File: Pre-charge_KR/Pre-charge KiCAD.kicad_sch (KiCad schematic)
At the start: 56 parts, among them IC1 AL5890-10D-13, IC2 TLV1701AIDBVT, J1 Conn_01x02, J113 Conn_01x06, J3 Conn_01x02, J4 Conn_01x02, K2 G5Q-1A4-DC12, K3 67-1-A-12/2D, Q1 2N7000, Q2 2N7000, Q4 2N7000, U1 HCPL-817-000E, U10 LM7805MPX/NOPB, U13 HCPL-817-000E, U2 LM339N/NOPB, U3 SN74AHCT1G08DBVR, U7 LM741CN/NOPB, U8 SN74AHC1G04DBVRE4

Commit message: breakout updated and ENNOID BMS added
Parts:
- removed Q1: 2N7000, Package_TO_SOT_THT:TO-92_Inline, symbol Transistor_FET:2N7000
- removed R11: 10k, Resistor_THT:R_Axial_DIN0207_L6.3mm_D2.5mm_P10.16mm_Horizontal, symbol Device:R_Small
- removed R9: 100, Resistor_THT:R_Axial_DIN0207_L6.3mm_D2.5mm_P10.16mm_Horizontal, symbol Device:R_Small
- renumbered J113 to J2
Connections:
- net Precharge_done/Close_AIR1: now also R8.1, U2.13
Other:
- note added: "AIR close should be shutdown ok and RTD OK and Precharge done"
- note added: "I have a feeling this relay resistor order is incorrect"
- note added: "Is this necessary or just good to have? theres no teensy monitoring pins setup right now for this"
- note added: "Precharge enable should be SDWN_PC and RTD and PC not done"
- note added: "Think this is a debug pin, but its the wrong voltage"
- note added: "This comes from Teensy"
- note added: "This goes to the AIR"
- note added: "This goes to the TSAL"
- note added: "This is end of shutdown circuit daisy chain"
- note added: "This should be 3.3V to not blow the Teensy"
- moved on the sheet: C10, C11, C2, C7, J2, J3, R24, U10, U8

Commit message: precharge complete
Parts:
- removed C1, C11: 0.1uF, FA14_Capacitor:FA18X7R1H104KNU00, symbol Device:C
- removed C2: 10uF, Capacitor_THT:CP_Radial_D5.0mm_P2.50mm, symbol Device:C_Polarized
- removed C4: 0.1uF, FA14_Capacitor:FA18X7R1H104KNU00, symbol Device:C_Small
- removed C7: 0.22uF, FA14_Capacitor:FA14X7R1H224KNU00, symbol Device:C
- removed D1: TZX3V9C-TAP, Diode_THT:D_DO-35_SOD27_P7.62mm_Horizontal, symbol Diode:BZX384-xxx
- removed D3: TZX3V0B-TR, Diode_THT:D_DO-35_SOD27_P7.62mm_Horizontal, symbol Diode:BZX384-xxx
- removed IC1: AL5890-10D-13, AL589010D13:AL589010D13, symbol AL5890-10D-13:AL5890-10D-13
- removed LED1: LTL-1CHG, LTL1CHG:LTL1CHG, symbol LTL-1CHG:LTL-1CHG
- removed R12: 20k, Resistor_THT:R_Axial_DIN0207_L6.3mm_D2.5mm_P10.16mm_Horizontal, symbol Device:R_Small
- removed R24: 1M, Resistor_THT:R_Axial_DIN0207_L6.3mm_D2.5mm_P10.16mm_Horizontal, symbol Device:R_Small
- removed R36: 6.8k, Resistor_THT:R_Axial_DIN0207_L6.3mm_D2.5mm_P10.16mm_Horizontal, symbol Device:R_Small
- removed R37: 4.7k, Resistor_THT:R_Axial_DIN0207_L6.3mm_D2.5mm_P10.16mm_Horizontal, symbol Device:R_Small
- removed U10: LM7805MPX/NOPB, Package_TO_SOT_SMD:SOT-223-3_TabPin2, symbol Regulator_Linear:LM7805_TO220
- removed U2: LM339N/NOPB, LM339N:DIP794W53P254L1930H508Q14N, symbol Comparator:LM339
- removed U3: SN74AHCT1G08DBVR, Package_TO_SOT_SMD:SOT-23-5, symbol 74xGxx:74AHC1G08
- removed U7: LM741CN/NOPB, Package_DIP:DIP-8_W7.62mm, symbol Amplifier_Operational:LM741
- added C1, C4: 1uF, FA14_Capacitor:FA18X7R1H104KNU00, symbol tsal-rescue:C_Small-Device
- added C2: 0.1uF, FA14_Capacitor:FA18X7R1H104KNU00, symbol Device:C
- added C5: 2.2uF, FA14_Capacitor:FA14X7R1H224KNU00, symbol Device:C_Small
- added D1: 1N4001, Diode_THT:D_DO-41_SOD81_P10.16mm_Horizontal, symbol Device:D
- added D2, D3: 1N4148, Diode_THT:D_DO-35_SOD27_P7.62mm_Horizontal, symbol Diode:1N4148
- added IC3: SN74LVC1G11DCKRE4, SOT65:SOT65P210X110-6N, symbol SN74LVC1G11DCKRE4:SN74LVC1G11DCKRE4
- added IC4: SN74LVC1G08IDCKRQ1, AND:SOT65P210X110-5N, symbol SN74LVC1G08IDCKRQ1:SN74LVC1G08IDCKRQ1
- added R10, R9: 56k, Resistor_THT:R_Axial_DIN0411_L9.9mm_D3.6mm_P12.70mm_Horizontal, symbol Device:R_Small
- added R11: 330, Resistor_THT:R_Axial_DIN0207_L6.3mm_D2.5mm_P10.16mm_Horizontal, symbol Device:R_Small
- added R3, R6: 100k, Resistor_THT:R_Axial_DIN0207_L6.3mm_D2.5mm_P10.16mm_Horizontal, symbol Device:R_Small
- added U2: MCP1703AT-3302E/MBVAO, Package_TO_SOT_SMD:SOT-89-3, symbol Regulator_Linear:MCP1703Ax-300xxMB
- J3: footprint Phoenix 1x2 Connector:Phoenix_1x2_1729128 -> Connector_JST:JST_XH_B2B-XH-A_1x02_P2.50mm_Vertical; Part Number 1729128 -> B6B-XH-A
- R1: value 1.5k -> 100k; Part Number MCF 0.25W 1K5 -> MCF 0.25W 100K
- R2: value 1.5k -> 1M; Part Number MCF 0.25W 1K5 -> MCF 0.25W 1M
- R32, R33, R7: value 10k -> 100k; Part Number MCF 0.25W 10K -> MCF 0.25W 100K
- R34: value 180k -> 1.8M; Part Number MCF 0.25W 180K -> MCF 0.25W 1.8M
- R35: value 1k -> 2.2k; Part Number MCF 0.25W 1K -> MCF 0.25W 2.2k
- R4: value 6.8k -> 10k; Part Number MCF 0.25W 6K8 -> MCF 0.25W 10k
- R5: value 4.7k -> 27k; Part Number MCF 0.25W 4K7 -> MCF 0.25W 27K
- R8: value 10k -> 56k; footprint Resistor_THT:R_Axial_DIN0207_L6.3mm_D2.5mm_P10.16mm_Horizontal -> Resistor_THT:R_Axial_DIN0411_L9.9mm_D3.6mm_P12.70mm_Horizontal; Part Number MCF 0.25W 10K -> MCF 0.5W 56K
- U8: value SN74AHC1G04DBVRE4 -> SN74LVC1G04QDBVRQ1; Part Number SN74AHC1G04DBVRE4 -> SN74LVC1G04QDBVRQ1
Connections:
- net 3Vref is gone; now on an unnamed net: R2.2
- net 12V_HV: now also R4.2
- net GLV+: now also C4.1, U2.2 (VI); no longer R1.1, R2.1, U1.4, U13.4
- net GND: now also J2.3 (Pin_3), R1.1, R7.1, C1.2, C2.2, C4.2, C5.1, IC3.2 (GND), IC4.3 (GND), R3.1, U2.1 (GND); no longer J2.6 (Pin_6), R5.2
- net PRE_RESIST+: now also R8.1
- net Precharge NOT done: now also U8.4, IC4.2 (B); no longer Q4.2 (G)
- net Precharge_ON: now also J2.6 (Pin_6), U1.3, R3.2; no longer J2.1 (Pin_1), R7.1
- net SDWN_PC: now also R5.2, D1.1 (K)
- net Shutdown_AIR1+: now also J2.1 (Pin_1); no longer J2.3 (Pin_3)
- net TS-: now also U1.2, D3.2 (A); no longer U13.2
- net Precharge_done: now reaches U13.3
- net Precharge_done: now also J2.4 (Pin_4), R1.2, U8.2, IC3.1 (A)
- net at R35.1, U13.1: no longer IC2.4 (OUT)
- net at R30.2, R31.1: now also IC2.3 (IN-); no longer IC2.1 (IN+)
- net at R32.1: now also R28.2, R29.1
- net at R32.2, R33.1: now also IC2.1 (IN+), R2.1; no longer IC2.3 (IN-)
- net at R13.2: now also R5.1, IC3.3 (B)
- net at R23.1: now also IC3.4 (Y)
- net at K3.3, Q4.3 (D): now also D1.2 (A)
- net at U1.1: now also D3.1 (K), R11.1
- net at R4.1: now also IC2.4 (OUT), U13.2; no longer U1.3
- removed net 3V9: R1.2, R7.2, R8.2
- net 5V renamed 3.3V
- net 3.3V: now also U1.4, U13.4, C1.1, C2.1, IC3.5 (VCC), IC4.5 (VCC), U2.3 (VO)
- removed net Precharge_done/Close_AIR1: J2.4 (Pin_4), R8.1, U8.2
- net TS_activate renamed Precharge_EN
- net Precharge_EN: now also IC3.6 (C), IC4.1 (A)
- new net: C5.2, D2.1 (K), Q4.2 (G), R6.1, R7.2
- new net: R8.2, R9.1
- new net: R10.1, R9.2
- new net: R10.2, R11.2
- new net: D2.2 (A), IC4.4 (Y), R6.2
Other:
- note added: "AIR_CLOSE_EN = SDC_OK AND RTD_OK AND PC_DONE"
- note added: "Isolated DCDC converter"
- note added: "PC_RELAY_EN = SDC_OK AND RTD_OK AND NOT PC_DONE"
- note added: "Preresist- is the node between resistor and motor inverter capacitor"
- note added: "This delay stops race condition of precharge closing and AIR opening unpredictably at the same time 220ms is orders of magnitude long enough"
- note added: "This goes to the AIR controller"
- note added: "This is for monitoring/debugging, most likely to esp32"
- note added: "debug pin"
- note added: "hysteresis resistor"
- note added: "when precharge voltage is greater than 95% of TS voltage, open drain comparator opens and sinks current, the optocoupler led turns on, and precharge done goes high"
- note removed: "AIR close should be shutdown ok and RTD OK and Precharge done"
- note removed: "I have a feeling this relay resistor order is incorrect"
- note removed: "Is this necessary or just good to have? theres no teensy monitoring pins setup right now for this"
- note removed: "Pre-Charge Relay Status"
- note removed: "Precharge enable should be SDWN_PC and RTD and PC not done"
- note removed: "The SDWN_PC must be included here because it is taking the voltage measurement between AIR1- and PRE_RESIST-. The SDWN signal for the Precharge Relay doesn't affect this part of the circuit, so it must be included here for the AIR"
- note removed: "Think this is a debug pin, but its the wrong voltage"
- note removed: "This goes to the AIR"
- note removed: "This needs to be Resist- or else the Precharge relay will go into an oscilatory loop of open and closed. Like this... Initial state: when precharge is not done, the relay closes, and opens after precharge is done. When the relay is open, Pre_RESIST+ would go LOW, ie Precharge not done is high, which will the close the relay again, putting it in a loop"
- note removed: "This should be 3.3V to not blow the Teensy"
- note removed: "when precharge voltage is greater than 95% of TS voltage, this output is high, and the AIR can close."
- note removed: "when the AIR gets a signal to close, a 10 second delay to opening the precharge relay ensures the the voltage measurement never dips, so for 10 seconds the AIR and precharge relay will both be closed. Then the precharge can open, and the AIR will remain closed."
- moved on the sheet: C10, C14, C3, C6, C9, D5, IC2, J1, J2, J3, J4, K2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

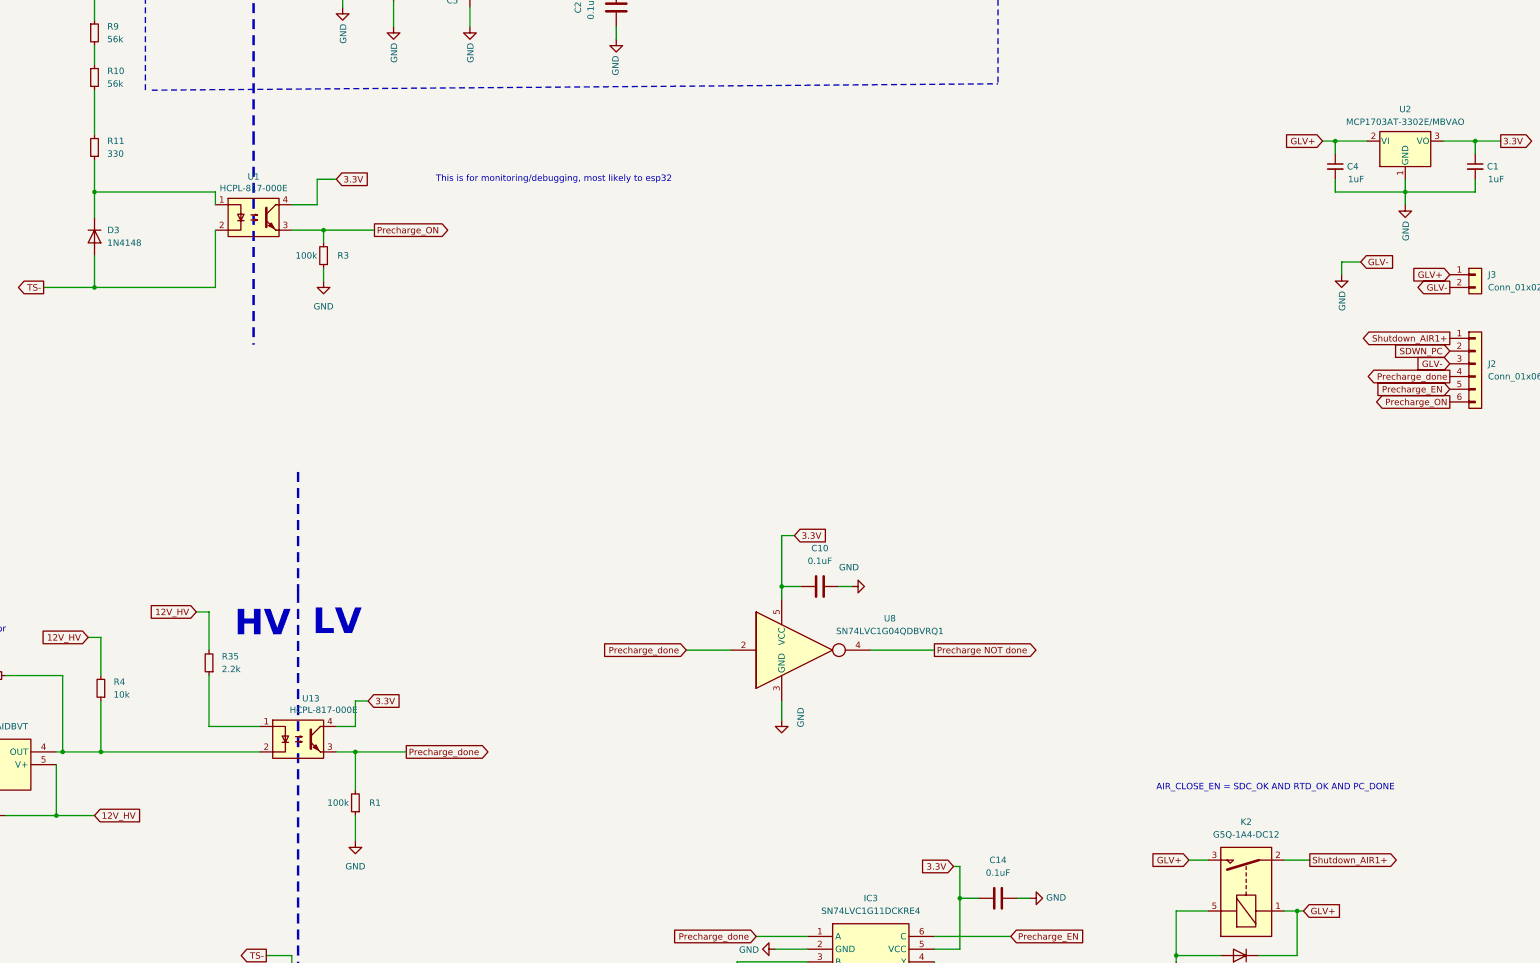
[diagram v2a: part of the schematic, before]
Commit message: precharge and discharge fixed
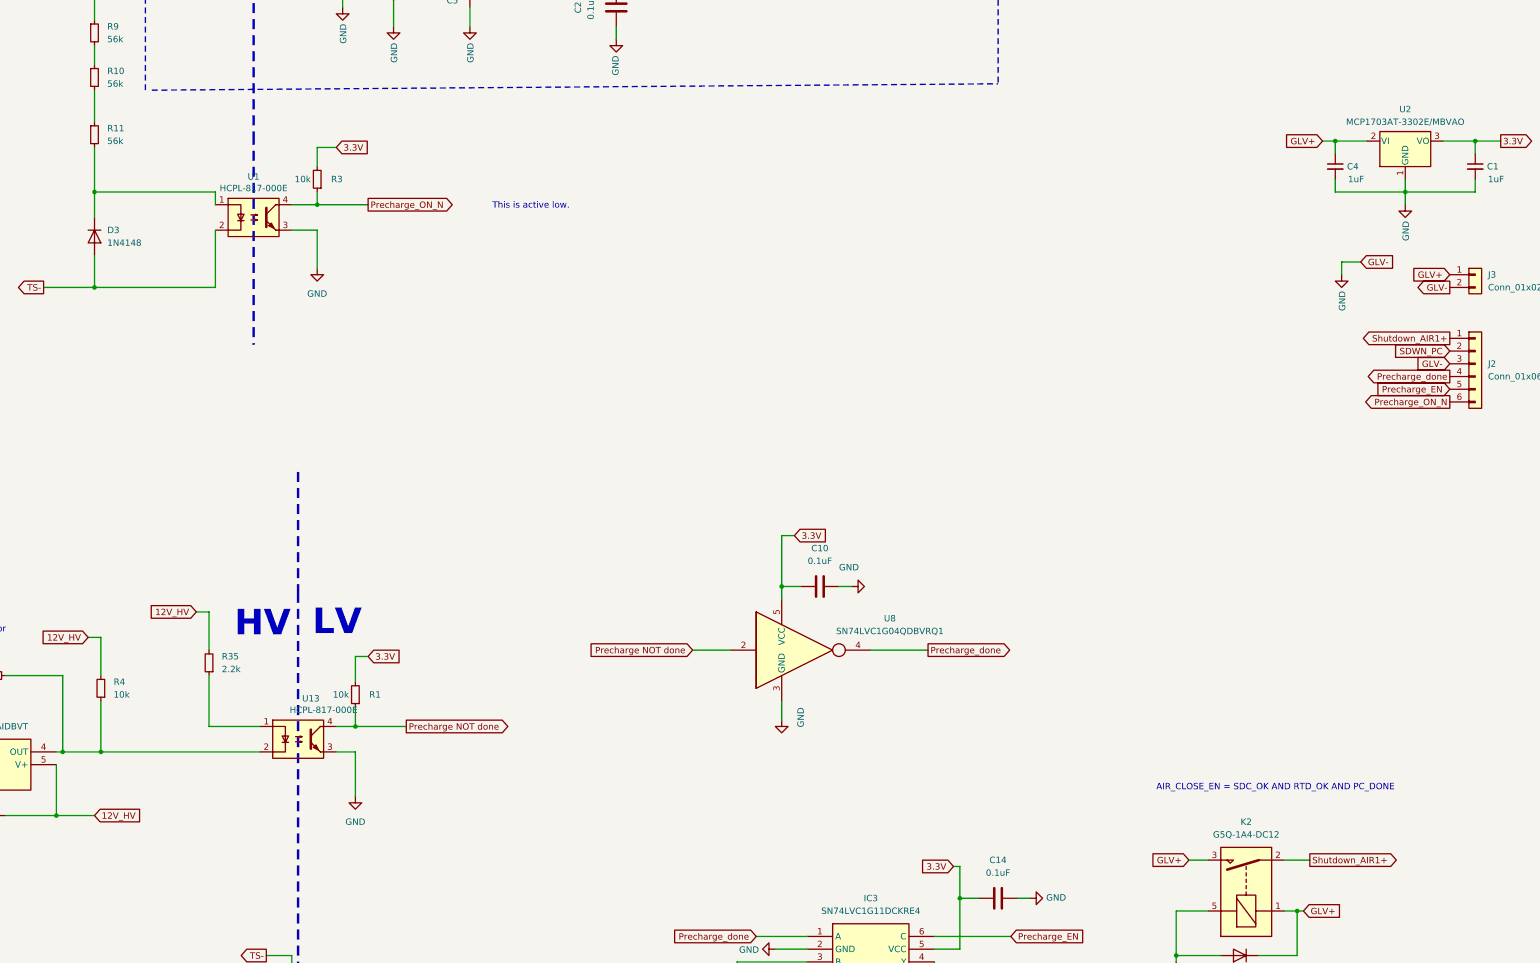
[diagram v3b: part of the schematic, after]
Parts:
- R1, R3: value 100k -> 10k; Part Number MCF 0.25W 100K -> MCF 0.25W 10K
- R11: value 330 -> 56k; footprint Resistor_THT:R_Axial_DIN0207_L6.3mm_D2.5mm_P10.16mm_Horizontal -> Resistor_THT:R_Axial_DIN0411_L9.9mm_D3.6mm_P12.70mm_Horizontal; Part Number MCF 0.25W 330 -> MCF 0.5W 56K
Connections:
- net 3.3V: now also R1.2, R3.2; no longer U1.4, U13.4
- net GND: now also U1.3, U13.3; no longer R1.1, R3.1
- net Precharge NOT done: now also R1.1, U13.4, U8.2; no longer U8.4
- net Precharge_done: now also U8.4; no longer R1.2, U13.3, U8.2
- net at R10.2: now also R11.1; no longer R11.2
- net at D3.1 (K), U1.1: now also R11.2; no longer R11.1
- removed net Precharge_ON: J2.6 (Pin_6), R3.2, U1.3
- new net Precharge_ON_N: J2.6 (Pin_6), R3.1, U1.4
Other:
- note added: "This is active low."
- note removed: "This is for monitoring/debugging, most likely to esp32"
- moved on the sheet: R3

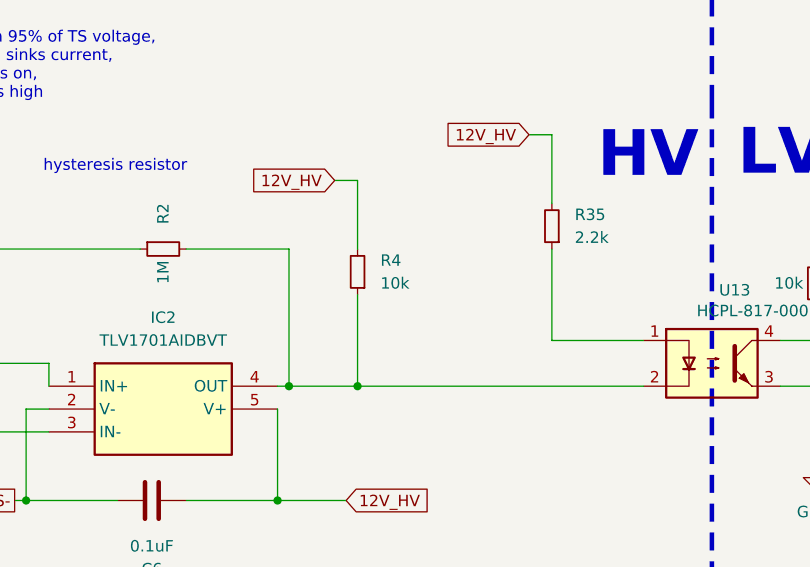
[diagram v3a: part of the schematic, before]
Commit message: Voltage measurement completed
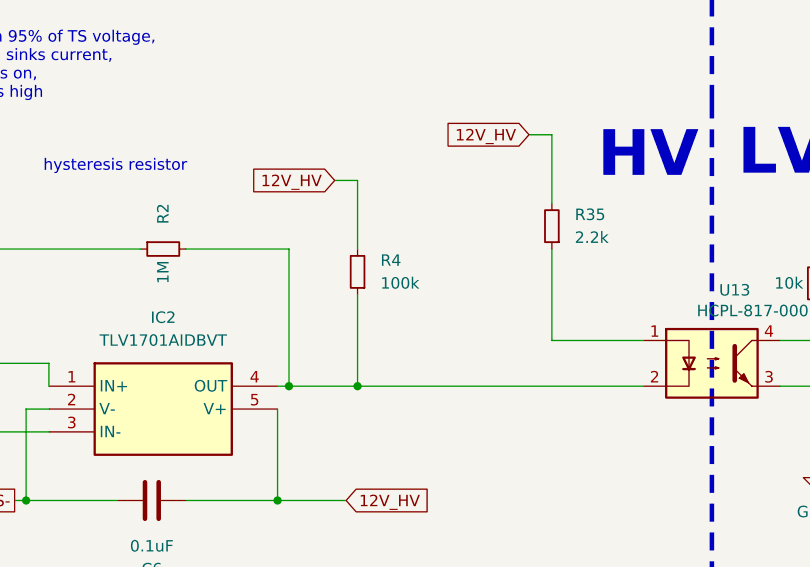
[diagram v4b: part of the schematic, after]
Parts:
- R4: value 10k -> 100k; Part Number MCF 0.25W 10k -> MCF 0.25W 100k
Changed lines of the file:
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@@
 		(rev "v10")
 		(company "UCD Formula Student")
-		(comment 1 "Original Author: Nebojša Cvetković")
-		(comment 2 "Amended by: Darren Garrett in 2022 V09")
-		(comment 3 "Amended by: Kieran Mcilreavy")
-		(comment 4 "Amended by: Rebecca McDonald ")
+		(comment 1 "Author: Keelan Reilly")
 	)
 	(text "This is end of shutdown circuit daisy chain"
@@
 			)
 		)
-		(property "Value" "10k"
+		(property "Value" "100k"
 			(at 162.56 287.0199 0)
 			(effects
@@
 			)
 		)
-		(property "Part Number" "MCF 0.25W 10k"
+		(property "Part Number" "MCF 0.25W 100k"
 			(at 160.02 285.75 0)
 			(effects

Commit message: ENNOID BMS PCBs completed
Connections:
- net PRE_RESIST-: no longer R30.1
- net TS-: no longer R31.2
- new net Load+: R30.1
- new net Load-: R31.2
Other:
- note added: "load+ is the node between resistor and motor inverter capacitor load- is the inverter side negative"
- note removed: "Preresist- is the node between resistor and motor inverter capacitor"
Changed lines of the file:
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@@
 		)
 	)
-	(text "Preresist- is the node between resistor and motor inverter capacitor"
+	(text "load+ is the node between resistor and motor inverter capacitor\nload- is the inverter side negative"
 		(exclude_from_sim no)
 		(at 83.82 355.6 0)
@@
 		)
 	)
-	(global_label "TS-"
+	(global_label "Load-"
 		(shape output)
 		(at 73.66 345.44 180)
@@
 		)
 		(property "Intersheetrefs" "${INTERSHEET_REFS}"
-			(at 66.8302 345.44 0)
+			(at 64.5322 345.44 0)
 			(effects
 				(font
@@
 		)
 	)
-	(global_label "PRE_RESIST-"
+	(global_label "Load+"
 		(shape input)
 		(at 72.39 322.58 180)
@@
 		)
 		(property "Intersheetrefs" "${INTERSHEET_REFS}"
-			(at 56.6703 322.58 0)
-			(effects
-				(font
+			(at 63.2622 322.58 0)
+			(effects
+				(font
